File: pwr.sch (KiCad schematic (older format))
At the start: 55 parts, among them U1 FT601, U10 MIC94310, U11 PAM2305, U4 ECP5, U6 PAM2305, U7 NCP186, U8 MIC94310, U9 MIC94310, X2 CONN_01X08

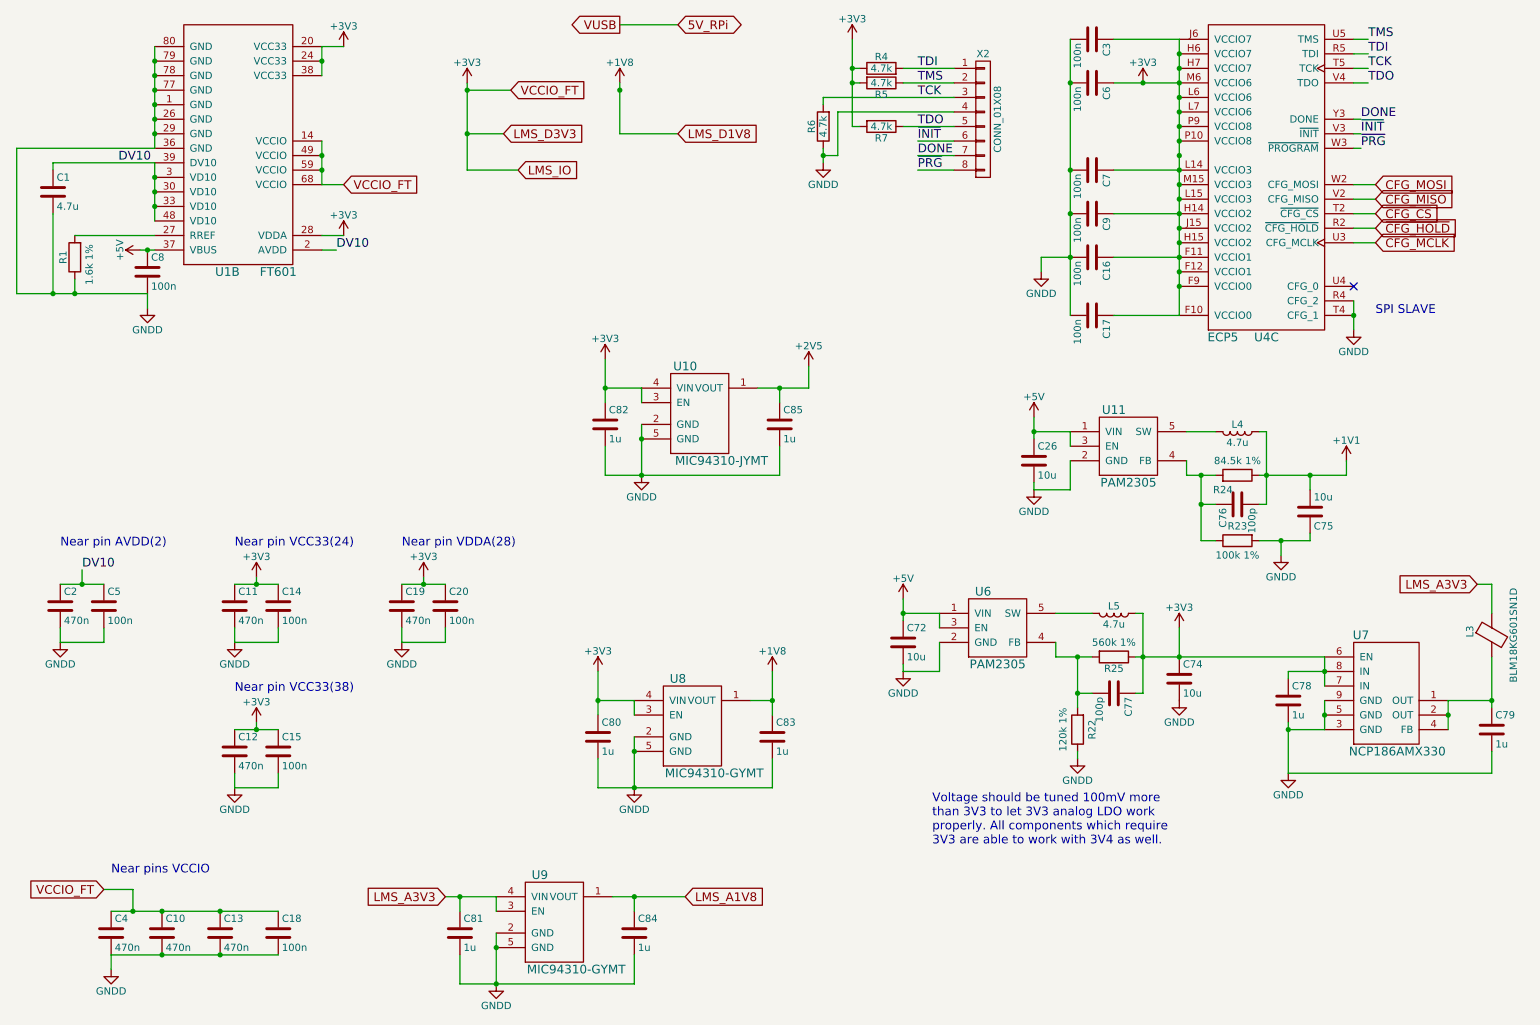
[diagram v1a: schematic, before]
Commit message: Placement of RF is on going.
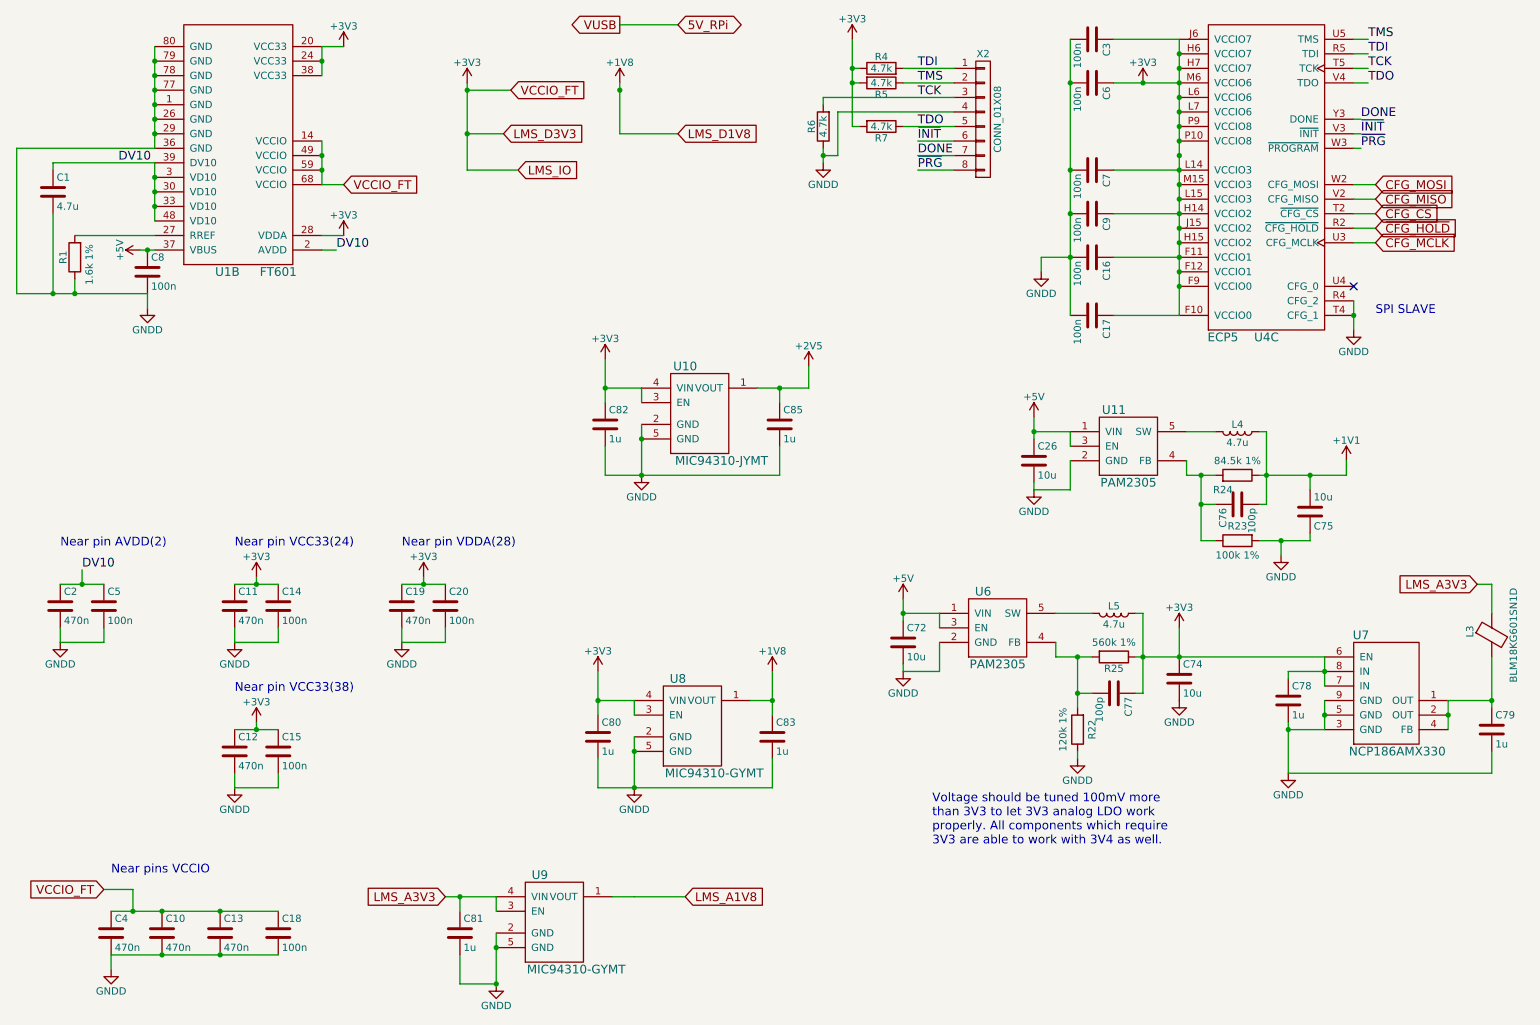
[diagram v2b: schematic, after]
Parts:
- removed C84: 1u, Capacitors_SMD:C_0603, symbol C

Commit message: Add jumpers for LMS power Traced most nets in LMS digital
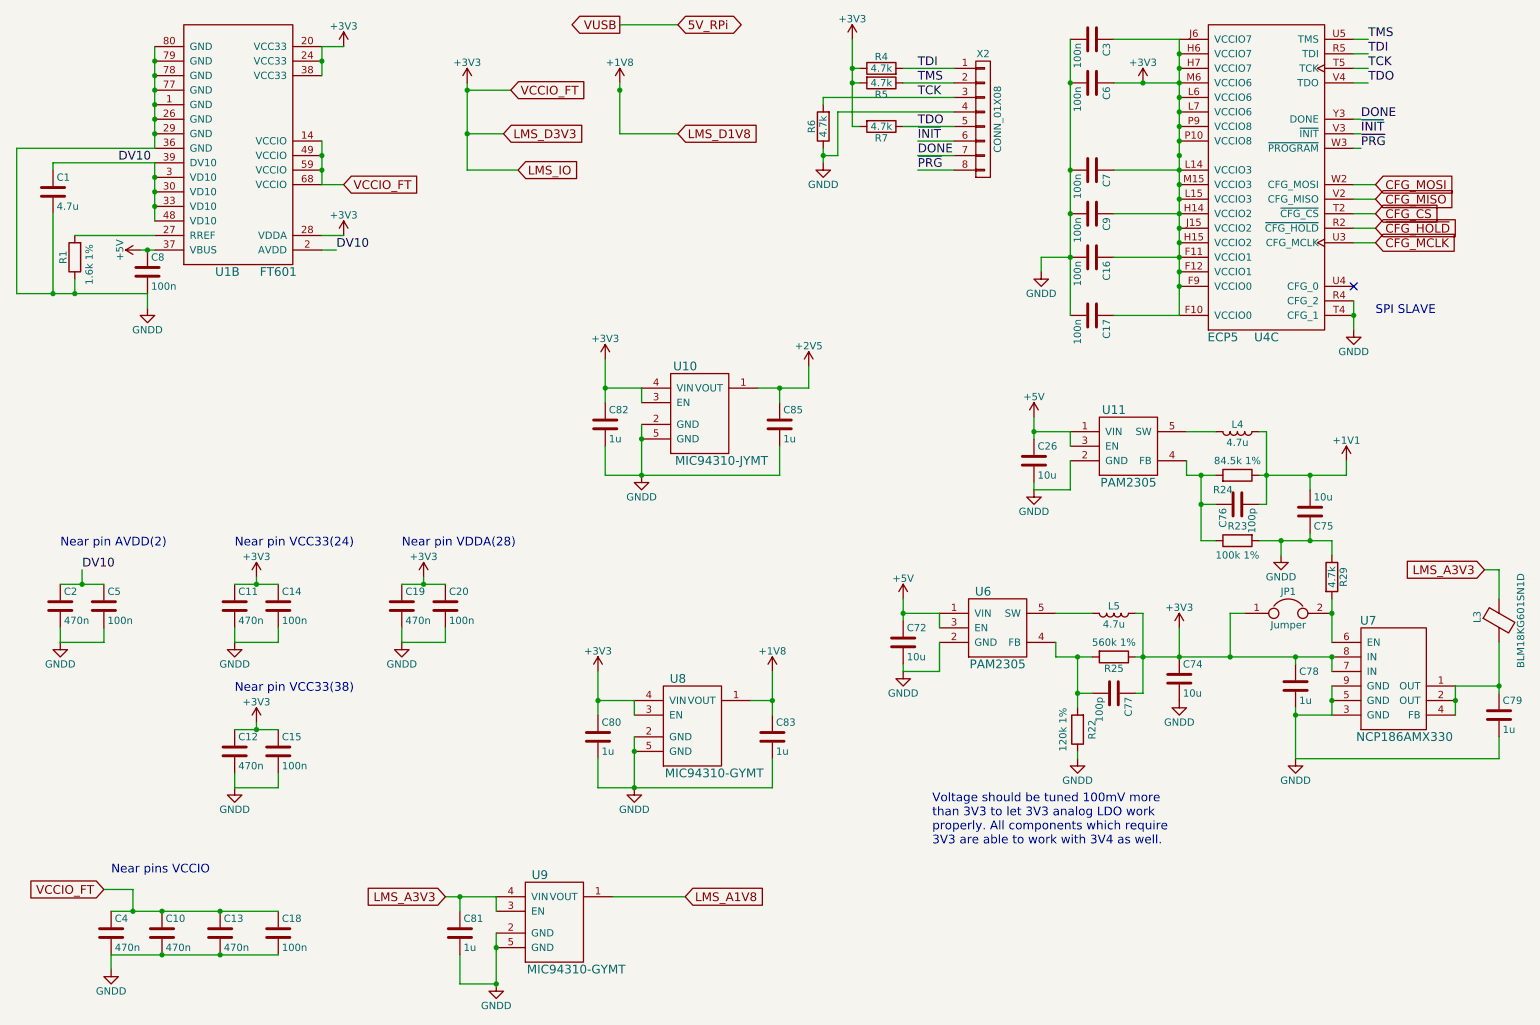
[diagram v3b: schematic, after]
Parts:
- added JP1: Jumper, Pin_Headers:Pin_Header_Straight_1x02_Pitch2.54mm, symbol Jumper
- added R29: 4.7k, Resistors_SMD:R_0603, symbol R
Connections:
- net +3V3: now also JP1.1; no longer U7.6 (EN)
- net GNDD: now also R29.1
- new net: JP1.2, R29.2, U7.6 (EN)
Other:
- moved on the sheet: C78, C79, L3, U7

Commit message: Placement of all passive is finished. Tracing of most passive is finished. RF is not started yet.
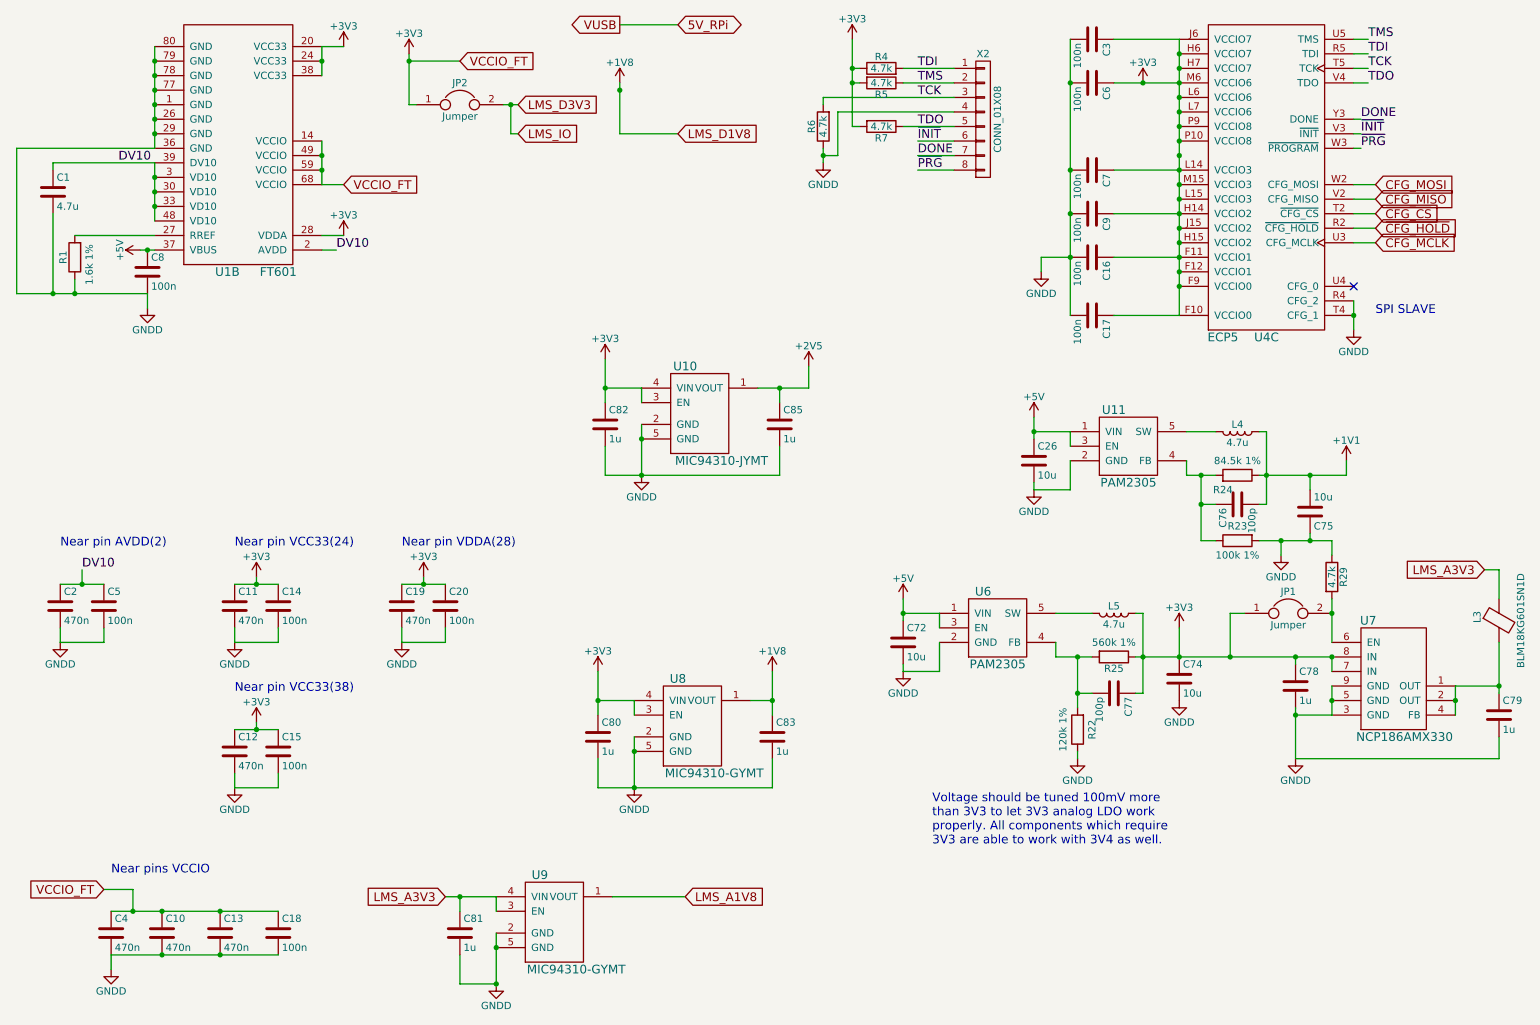
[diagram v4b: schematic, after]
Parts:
- added JP2: Jumper, Pin_Headers:Pin_Header_Straight_1x02_Pitch2.54mm, symbol Jumper
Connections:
- net +3V3: now also JP2.1
- new net LMS_D3V3: JP2.2
